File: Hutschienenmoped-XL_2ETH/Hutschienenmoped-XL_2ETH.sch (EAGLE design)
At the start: 129 parts, among them J1 638207222005, J13 638207222005, J15 638207222008, J2 645004114822, J4 61300421121, J7 638207222005, J8 638207222007, U4 TLE9250VSJ

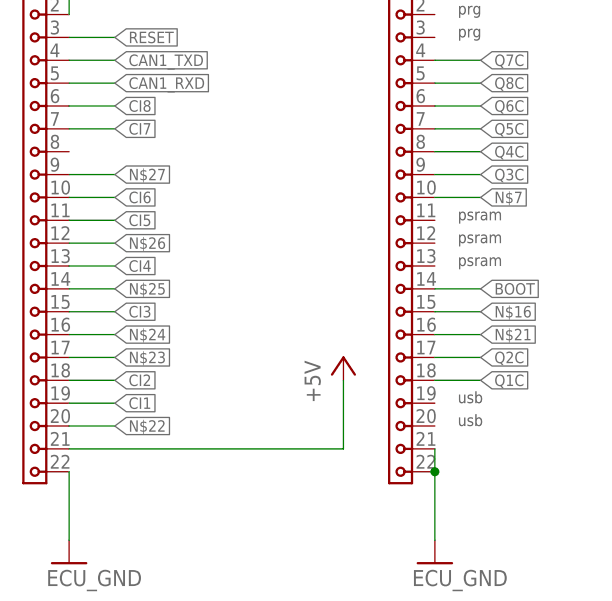
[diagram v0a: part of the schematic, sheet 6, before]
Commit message: Update layer visibility settings and pad dimensions. Adjusted layer visibility to improve clarity. Increased maximum pad sizes for top and bottom layers from 0.5mm to 1mm for better functionality. Modified thermal isolation setting from 0.2mm to 0.45mm for improved performance in PCB design.
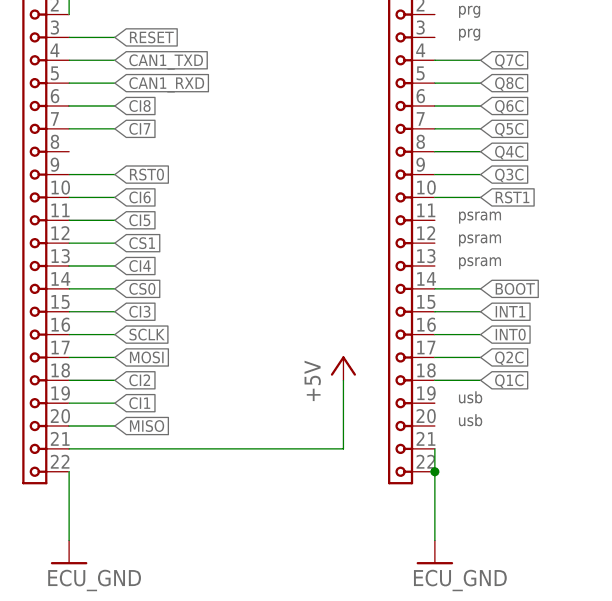
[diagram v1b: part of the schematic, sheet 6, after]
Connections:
- removed net N$16: ESP32-J3.15
- removed net N$21: ESP32-J3.16
- removed net N$22: ESP32-J1.20
- removed net N$23: ESP32-J1.17
- removed net N$24: ESP32-J1.16
- removed net N$25: ESP32-J1.14
- removed net N$26: ESP32-J1.12
- removed net N$27: ESP32-J1.9
- removed net N$7: ESP32-J3.10
- net CS0: now also ESP32-J1.14
- net CS1: now also ESP32-J1.12
- net INT0: now also ESP32-J3.16
- net INT1: now also ESP32-J3.15
- net MISO: now also ESP32-J1.20
- net MOSI: now also ESP32-J1.17
- net RST0: now also ESP32-J1.9
- net RST1: now also ESP32-J3.10
- net SCLK: now also ESP32-J1.16
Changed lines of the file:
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@@
 </segment>
 </net>
-<net name="N$7" class="0">
+<net name="RST1" class="0">
 <segment>
 <pinref part="ESP32-J3" gate="G$1" pin="10"/>
@@
 </segment>
 </net>
-<net name="N$16" class="0">
+<net name="INT1" class="0">
 <segment>
 <pinref part="ESP32-J3" gate="G$1" pin="15"/>
@@
 </segment>
 </net>
-<net name="N$21" class="0">
+<net name="INT0" class="0">
 <segment>
 <pinref part="ESP32-J3" gate="G$1" pin="16"/>
@@
 </segment>
 </net>
-<net name="N$22" class="0">
+<net name="MISO" class="0">
 <segment>
 <pinref part="ESP32-J1" gate="G$1" pin="20"/>
@@
 </segment>
 </net>
-<net name="N$23" class="0">
+<net name="MOSI" class="0">
 <segment>
 <pinref part="ESP32-J1" gate="G$1" pin="17"/>
@@
 </segment>
 </net>
-<net name="N$24" class="0">
+<net name="SCLK" class="0">
 <segment>
 <pinref part="ESP32-J1" gate="G$1" pin="16"/>
@@
 </segment>
 </net>
-<net name="N$25" class="0">
+<net name="CS0" class="0">
 <segment>
 <pinref part="ESP32-J1" gate="G$1" pin="14"/>
@@
 </segment>
 </net>
-<net name="N$26" class="0">
+<net name="CS1" class="0">
 <segment>
 <pinref part="ESP32-J1" gate="G$1" pin="12"/>
@@
 </segment>
 </net>
-<net name="N$27" class="0">
+<net name="RST0" class="0">
 <segment>
 <pinref part="ESP32-J1" gate="G$1" pin="9"/>

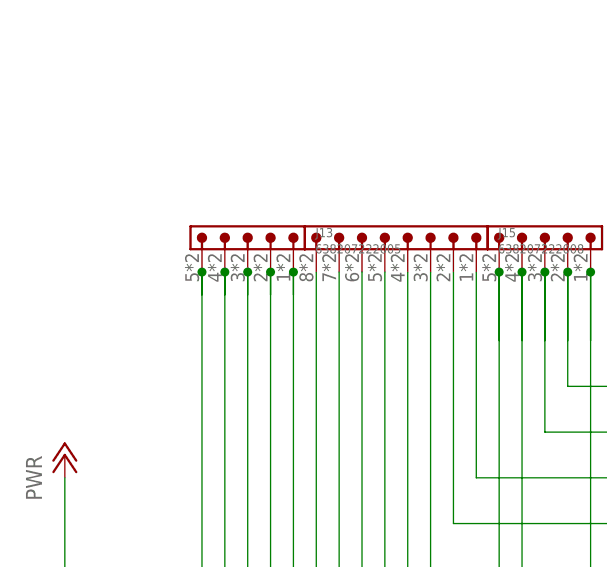
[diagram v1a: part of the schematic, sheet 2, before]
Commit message: Change grid unit from mil to mm, adjust polygon width, add contact references for elements J13 and J9, update via drill sizes, modify wire connections for various signals.
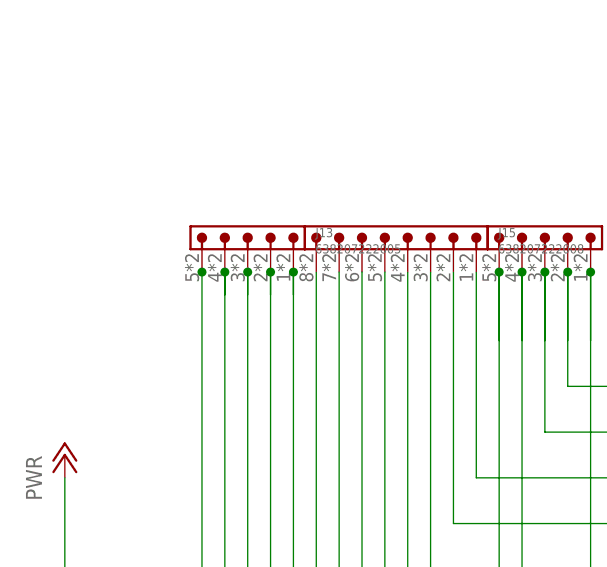
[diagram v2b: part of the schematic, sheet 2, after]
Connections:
- removed net N$20: J13.5
- net PWR_GND: now also J13.5
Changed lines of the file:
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@@
 <pinref part="J15" gate="G$1" pin="7"/>
+</segment>
+<segment>
+<pinref part="J13" gate="G$1" pin="5"/>
+<pinref part="PWR_GND2" gate="PWR_GND" pin="PWR_GND"/>
+<wire x1="-30.48" y1="96.52" x2="-30.48" y2="38.1" width="0.1524" layer="91"/>
+<junction x="-30.48" y="96.52"/>
 </segment>
 </net>
@@
 </segment>
 </net>
-<net name="N$20" class="0">
-<segment>
-<wire x1="-30.48" y1="96.52" x2="-30.48" y2="38.1" width="0.1524" layer="91"/>
-<pinref part="PWR_GND2" gate="PWR_GND" pin="PWR_GND"/>
-<pinref part="J13" gate="G$1" pin="5"/>
-<junction x="-30.48" y="96.52"/>
-<wire x1="-30.48" y1="96.52" x2="-30.48" y2="93.98" width="0.1524" layer="91"/>
-</segment>
-</net>

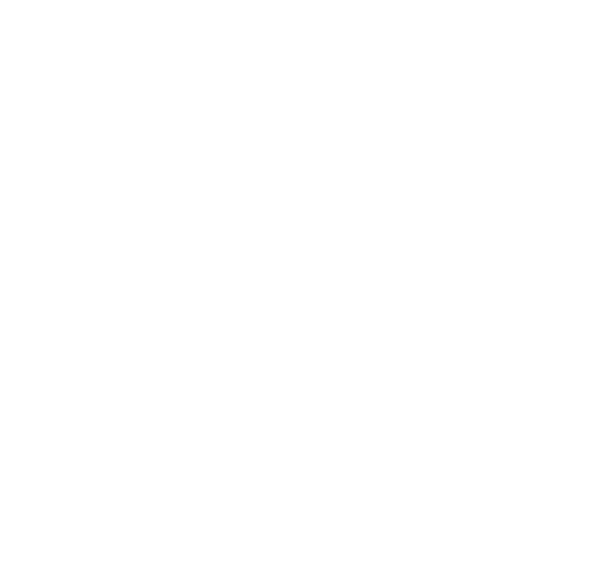
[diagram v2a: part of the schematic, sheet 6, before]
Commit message: Add resistors R14 and R15, update wiring connections. - Added resistors R14 and R15 with values of 13K. - Updated wiring connections for resistors R14 and R15 in the schematic and board files.
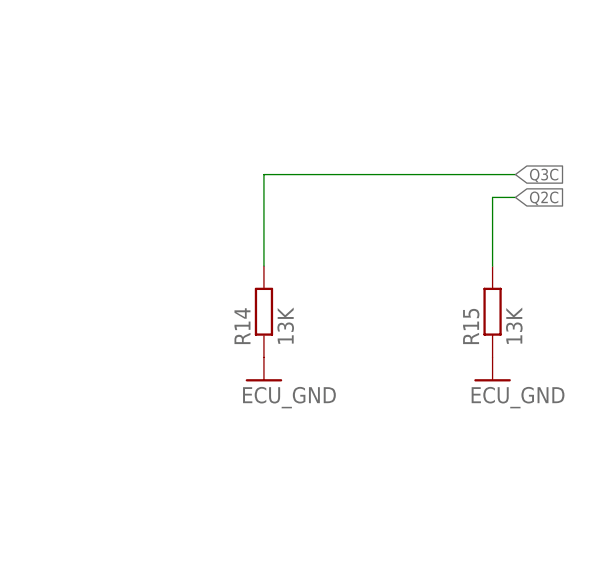
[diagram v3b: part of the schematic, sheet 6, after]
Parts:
- added R14, R15: 13K, resistor:R-EU_R1206
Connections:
- net ECU_GND: now also R14.1, R15.1
- net Q2C: now also R15.2
- net Q3C: now also R14.2
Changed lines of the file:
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@@
 <part name="+3V6" library="supply1" library_urn="urn:adsk.eagle:library:371" deviceset="+3V3" device=""/>
 <part name="ECU_GND38" library="supply_isobus" deviceset="ECU_GND" device=""/>
+<part name="R14" library="resistor" library_urn="urn:adsk.eagle:library:348" deviceset="R-EU_" device="R1206" package3d_urn="urn:adsk.eagle:package:23540/2" value="13K"/>
+<part name="R15" library="resistor" library_urn="urn:adsk.eagle:library:348" deviceset="R-EU_" device="R1206" package3d_urn="urn:adsk.eagle:package:23540/2" value="13K"/>
+<part name="ECU_GND39" library="supply_isobus" deviceset="ECU_GND" device=""/>
+<part name="ECU_GND40" library="supply_isobus" deviceset="ECU_GND" device=""/>
 </parts>
 <sheets>
@@
 <attribute name="VALUE" x="132.08" y="83.82" size="1.778" layer="96" rot="R90"/>
 </instance>
+<instance part="R14" gate="G$1" x="198.12" y="106.68" smashed="yes" rot="R90">
+<attribute name="NAME" x="196.6214" y="102.87" size="1.778" layer="95" rot="R90"/>
+<attribute name="VALUE" x="201.422" y="102.87" size="1.778" layer="96" rot="R90"/>
+</instance>
+<instance part="R15" gate="G$1" x="223.52" y="106.68" smashed="yes" rot="R90">
+<attribute name="NAME" x="222.0214" y="102.87" size="1.778" layer="95" rot="R90"/>
+<attribute name="VALUE" x="226.822" y="102.87" size="1.778" layer="96" rot="R90"/>
+</instance>
+<instance part="ECU_GND39" gate="ECU_GND" x="198.12" y="99.06" smashed="yes">
+<attribute name="VALUE" x="195.58" y="96.52" size="1.778" layer="96"/>
+</instance>
+<instance part="ECU_GND40" gate="ECU_GND" x="223.52" y="99.06" smashed="yes">
+<attribute name="VALUE" x="220.98" y="96.52" size="1.778" layer="96"/>
+</instance>
 </instances>
 <busses>
@@
 <label x="149.86" y="88.9" size="1.27" layer="95" xref="yes"/>
 </segment>
+<segment>
+<pinref part="R15" gate="G$1" pin="2"/>
+<wire x1="223.52" y1="111.76" x2="223.52" y2="119.38" width="0.1524" layer="91"/>
+<wire x1="223.52" y1="119.38" x2="226.06" y2="119.38" width="0.1524" layer="91"/>
+<label x="226.06" y="119.38" size="1.27" layer="95" xref="yes"/>
+</segment>
 </net>
 <net name="CI3" class="0">
@@
 <pinref part="ECU_GND32" gate="ECU_GND" pin="ECU_GND"/>
 </segment>
+<segment>
+<pinref part="R14" gate="G$1" pin="1"/>
+<pinref part="ECU_GND39" gate="ECU_GND" pin="ECU_GND"/>
+</segment>
+<segment>
+<pinref part="R15" gate="G$1" pin="1"/>
+<pinref part="ECU_GND40" gate="ECU_GND" pin="ECU_GND"/>
+</segment>
 </net>
 <net name="CI4" class="0">
@@
 <label x="149.86" y="109.22" size="1.27" layer="95" xref="yes"/>
 </segment>
-</net>
+<segment>
+<pinref part="R14" gate="G$1" pin="2"/>
+<wire x1="198.12" y1="111.76" x2="198.12" y2="121.92" width="0.1524" layer="91"/>
+<wire x1="198.12" y1="121.92" x2="226.06" y2="121.92" width="0.1524" layer="91"/>
+<label x="226.06" y="121.92" size="1.27" layer="95" xref="yes"/>
+</segment>
+</net>
